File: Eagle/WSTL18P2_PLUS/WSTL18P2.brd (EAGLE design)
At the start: 44.1 x 23.6 mm, 30 parts, among them CON1 1X6CONN-1.27-ROUND_CENTERED, CON2 1X6CONN-1.27-ROUND_CENTERED, CON3 1X6CONN-1.27-ROUND_CENTERED, CON4 1X6CONN-1.27-ROUND_CENTERED, J3 FEMALE 2x3, T1 ABS07AIG

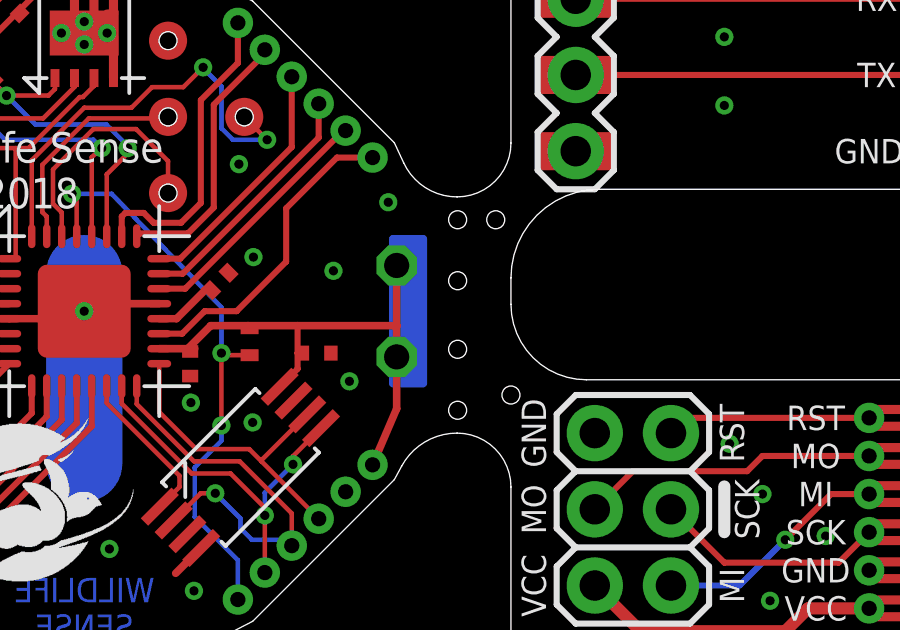
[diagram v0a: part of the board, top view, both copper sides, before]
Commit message: Removed a couple of diagrams to reorganize them
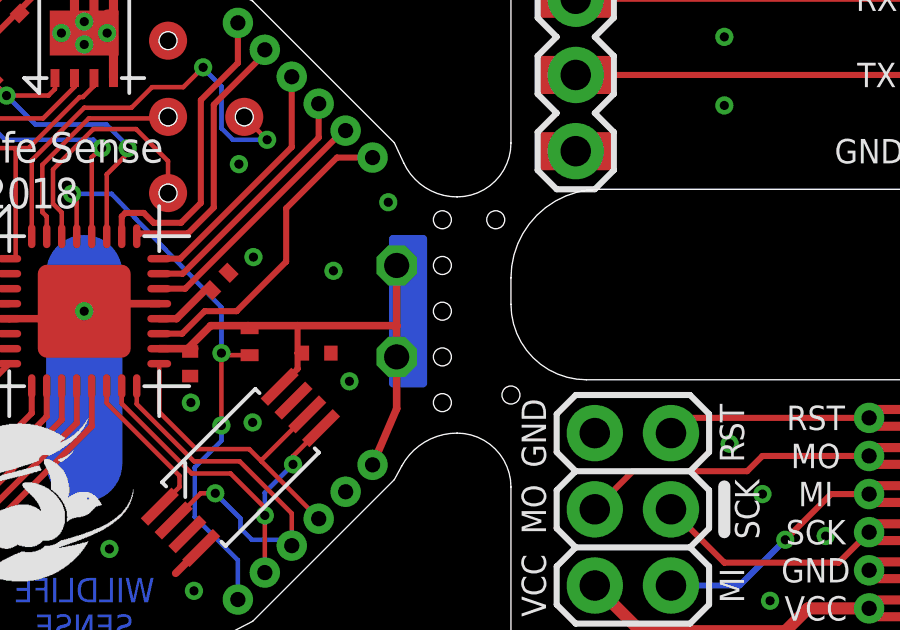
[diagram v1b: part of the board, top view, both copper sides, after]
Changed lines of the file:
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@@
 <hole x="16.002" y="17.145" drill="0.6"/>
 <wire x1="18.8214" y1="2.8702" x2="23.5458" y2="7.5946" width="0.0254" layer="20"/>
-<hole x="25.654" y="16.256" drill="0.6"/>
+<hole x="25.146" y="16.256" drill="0.6"/>
 <wire x1="23.5458" y1="7.5946" x2="23.7883" y2="8.04285625" width="0.0254" layer="20"/>
 <wire x1="23.7883" y1="8.04285625" x2="25.63595" y2="9.144" width="0.0254" layer="20" curve="-61.587374"/>
@@
 <wire x1="25.63595" y1="17.018" x2="23.85631875" y2="18.153315625" width="0.0254" layer="20" curve="-65.071676"/>
 <wire x1="23.85631875" y1="18.153315625" x2="23.5458" y2="18.8214" width="0.0254" layer="20"/>
-<hole x="25.654" y="14.224" drill="0.6"/>
-<hole x="25.654" y="11.938" drill="0.6"/>
-<hole x="25.654" y="9.906" drill="0.6"/>
+<hole x="25.146" y="14.732" drill="0.6"/>
+<hole x="25.146" y="11.684" drill="0.6"/>
+<hole x="25.146" y="10.16" drill="0.6"/>
 <hole x="26.924" y="16.256" drill="0.6"/>
 <hole x="27.432" y="10.414" drill="0.6"/>
@@
 <text x="39.624" y="21.082" size="0.8128" layer="21" font="vector" ratio="12" align="center">TX</text>
 <text x="39.624" y="23.622" size="0.8128" layer="21" font="vector" ratio="12" align="center">RX</text>
+<hole x="25.146" y="13.208" drill="0.6"/>
 </plain>
 <attributes>
